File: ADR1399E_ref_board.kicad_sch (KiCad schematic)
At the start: 89 parts, among them J1 Conn_01x02_Pin, J2 USB_C_Receptacle_PowerOnly_6P, J3 Conn_Coaxial, J4 S4B-XH-A, P1 JST_B2P_VH, Q1 MMBT3906, U1 LT3042xMSE, U2 TPS61085DGK, U3 TL331, U4 ADR1399KEZ, U5 LMT01LPG, U6 OPA182IDR, U7 OPA994IDR

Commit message: Final BOM (?)
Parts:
- added C1, C22: 1uF 25V, Capacitor_SMD:C_0603_1608Metric_Pad1.08x0.95mm_HandSolder, symbol Device:C
- added D3, D4: LED, LED_SMD:LED_1206_3216Metric_Pad1.42x1.75mm_HandSolder, symbol Device:LED
- added R10: 0R, Resistor_SMD:R_0805_2012Metric_Pad1.20x1.40mm_HandSolder, symbol Device:R
- added R24: 180k 0.1%, Resistor_SMD:R_0603_1608Metric_Pad0.98x0.95mm_HandSolder, symbol Device:R
- added R28, R29: 1.5k 1/4W, Resistor_SMD:R_1206_3216Metric_Pad1.30x1.75mm_HandSolder, symbol Device:R
- C10: renamed from C9; Manufacturer_Name (none) -> Samsung Electro-Mechanics; Manufacturer_Part_Number (none) -> CL32A106KBJNNNE
- C11: renamed from C10; Manufacturer_Name (none) -> Samsung Electro-Mechanics; Manufacturer_Part_Number (none) -> CL32A106KBJNNNE
- C12: renamed from C11; value 100n 50V -> 100nF 50V; Manufacturer_Name (none) -> Samsung Electro-Mechanics; Manufacturer_Part_Number (none) -> CL10B104KB8NNWC
- C13: renamed from C12; Manufacturer_Name (none) -> Samsung Electro-Mechanics; Manufacturer_Part_Number (none) -> CL32A106KBJNNNE
- C14: renamed from C13; Manufacturer_Name (none) -> YAGEO; Manufacturer_Part_Number (none) -> CC0603JRNPO9BN821
- C15: renamed from C23; Manufacturer_Name (none) -> TAIYO YUDEN; Manufacturer_Part_Number (none) -> TMK107ABJ225KA-T
- C16: renamed from C24; value 100n 50V -> 100nF 50V; Manufacturer_Name (none) -> Samsung Electro-Mechanics; Manufacturer_Part_Number (none) -> CL10B104KB8NNWC
- C17: renamed from C14; value 100n 50V -> 100nF 50V; Manufacturer_Name (none) -> Samsung Electro-Mechanics; Manufacturer_Part_Number (none) -> CL10B104KB8NNWC
- C18: renamed from C15; Manufacturer_Name (none) -> TAIYO YUDEN; Manufacturer_Part_Number (none) -> TMK107ABJ225KA-T
- C19: Manufacturer_Name (none) -> TAIYO YUDEN; Manufacturer_Part_Number (none) -> TMK107ABJ225KA-T
- C2: renamed from C1; Manufacturer_Name (none) -> Samsung Electro-Mechanics; Manufacturer_Part_Number (none) -> CL21A106KPFNNNG
- C20: renamed from C16; value 100n 50V -> 100nF 50V; Manufacturer_Name (none) -> Samsung Electro-Mechanics; Manufacturer_Part_Number (none) -> CL10B104KB8NNWC
- C21: renamed from C17; Manufacturer_Name (none) -> TAIYO YUDEN; Manufacturer_Part_Number (none) -> TMK107ABJ225KA-T
- C23: renamed from C21; Manufacturer_Name (none) -> Murata; Manufacturer_Part_Number (none) -> GCM1885C1H302JA16D
- C24: renamed from C20; Manufacturer_Name (none) -> KEMET; Manufacturer_Part_Number (none) -> C0603C102J5GAC7411
- C3: renamed from C2; Manufacturer_Name (none) -> Samsung Electro-Mechanics; Manufacturer_Part_Number (none) -> CL21A106KPFNNNG
- C4: renamed from C3; Manufacturer_Name (none) -> Samsung Electro-Mechanics; Manufacturer_Part_Number (none) -> CL21A106KPFNNNG
- C5: renamed from C4; value 330n 50V -> 100nF 50V; Manufacturer_Name (none) -> Samsung Electro-Mechanics; Manufacturer_Part_Number (none) -> CL10B104KB8NNWC
- C6: renamed from C5; Manufacturer_Name (none) -> Samsung Electro-Mechanics; Manufacturer_Part_Number (none) -> CL32A106KBJNNNE
- C7: renamed from C6; Manufacturer_Name (none) -> KEMET; Manufacturer_Part_Number (none) -> A768KE157M1ELAE029
- C8: renamed from C7; value 330n 50V -> 100nF 50V; Manufacturer_Name (none) -> Samsung Electro-Mechanics; Manufacturer_Part_Number (none) -> CL10B104KB8NNWC
- C9: renamed from C8; Manufacturer_Name (none) -> Samsung Electro-Mechanics; Manufacturer_Part_Number (none) -> CL32A106KBJNNNE
- CR1, CR2, CR3: Manufacturer_Name (none) -> Toshiba; Manufacturer_Part_Number (none) -> CMS06(TE12L,Q,M)
- D1: Manufacturer_Name (none) -> Inolux; Manufacturer_Part_Number (none) -> IN-S126ATA
- J2: Manufacturer_Name (none) -> GCT; Manufacturer_Part_Number (none) -> USB4125-GF-A-0190
- J3: Manufacturer_Name (none) -> Molex; Manufacturer_Part_Number (none) -> 73251-1150
- J4: Manufacturer_Name (none) -> JST; Manufacturer_Part_Number (none) -> S4B-XH-A-GU
- L1: Manufacturer_Name (none) -> ABRACON; Manufacturer_Part_Number (none) -> ASPI-6045S-120M-T
- L2: Manufacturer_Name (none) -> TAIYO YUDEN; Manufacturer_Part_Number (none) -> LBC3225T1R5MR
- P1: Manufacturer_Name (none) -> JST; Manufacturer_Part_Number (none) -> B2P-VH-GU
- Q1: Manufacturer_Name (none) -> OnSemi; Manufacturer_Part_Number (none) -> MMBT3906LT1G
- R1: value 10k -> 10k 0.5% 25ppm; footprint Resistor_SMD:R_0805_2012Metric_Pad1.20x1.40mm_HandSolder -> Resistor_SMD:R_0603_1608Metric_Pad0.98x0.95mm_HandSolder; Manufacturer_Name (none) -> Vishay; Manufacturer_Part_Number (none) -> MCT06030D1002DP500
- R11: renamed from R19; Manufacturer_Name (none) -> Vishay; Manufacturer_Part_Number (none) -> MCU0805MZ0000ZP500
- R12: renamed from R20; Manufacturer_Name (none) -> Susumu; Manufacturer_Part_Number (none) -> RR1220Q-100-D
- R13: renamed from R12; value 200k -> 180k 0.1%; footprint Resistor_SMD:R_0805_2012Metric_Pad1.20x1.40mm_HandSolder -> Resistor_SMD:R_0603_1608Metric_Pad0.98x0.95mm_HandSolder; Manufacturer_Name (none) -> Panasonic; Manufacturer_Part_Number (none) -> ERA-3AEB184V
- R14: renamed from R10; footprint Resistor_SMD:R_0805_2012Metric_Pad1.20x1.40mm_HandSolder -> Resistor_SMD:R_0603_1608Metric_Pad0.98x0.95mm_HandSolder; Manufacturer_Name (none) -> KOA Speer; Manufacturer_Part_Number (none) -> RN73R1JTTD1004B25
- R15: renamed from R11; value 1.5k -> 1.5k 1/4W; footprint Resistor_SMD:R_0805_2012Metric_Pad1.20x1.40mm_HandSolder -> Resistor_SMD:R_1206_3216Metric_Pad1.30x1.75mm_HandSolder; Manufacturer_Name (none) -> SEI Stackpole; Manufacturer_Part_Number (none) -> RNCP1206FTD1K50
- R16: renamed from R13; footprint Resistor_SMD:R_0805_2012Metric_Pad1.20x1.40mm_HandSolder -> Resistor_SMD:R_0603_1608Metric_Pad0.98x0.95mm_HandSolder; Manufacturer_Name (none) -> KOA Speer; Manufacturer_Part_Number (none) -> RN73R1JTTD1004B25
- R17: renamed from R14; footprint Resistor_SMD:R_0805_2012Metric_Pad1.20x1.40mm_HandSolder -> Resistor_SMD:R_0603_1608Metric_Pad0.98x0.95mm_HandSolder; Manufacturer_Name (none) -> KOA Speer; Manufacturer_Part_Number (none) -> RN73R1JTTD1004B25
- R18: renamed from R22; Manufacturer_Name (none) -> YAGEO; Manufacturer_Part_Number (none) -> RT0805BRD071RL
- R19: renamed from R16; value 366k -> 180k 0.1%; footprint Resistor_SMD:R_0805_2012Metric_Pad1.20x1.40mm_HandSolder -> Resistor_SMD:R_0603_1608Metric_Pad0.98x0.95mm_HandSolder; Manufacturer_Name (none) -> Panasonic; Manufacturer_Part_Number (none) -> ERA-3AEB184V
- R2, R3: value 366k -> 180k 0.1%; footprint Resistor_SMD:R_0805_2012Metric_Pad1.20x1.40mm_HandSolder -> Resistor_SMD:R_0603_1608Metric_Pad0.98x0.95mm_HandSolder; Manufacturer_Name (none) -> Panasonic; Manufacturer_Part_Number (none) -> ERA-3AEB184V
- R20: renamed from R17; footprint Resistor_SMD:R_0805_2012Metric_Pad1.20x1.40mm_HandSolder -> Resistor_SMD:R_0603_1608Metric_Pad0.98x0.95mm_HandSolder; Manufacturer_Name (none) -> KOA Speer; Manufacturer_Part_Number (none) -> RN73R1JTTD1004B25
- R21: renamed from R24; value 10k 0.1% 10ppm -> 10k 0.5% 25ppm; footprint Resistor_SMD:R_0805_2012Metric_Pad1.20x1.40mm_HandSolder -> Resistor_SMD:R_0603_1608Metric_Pad0.98x0.95mm_HandSolder; Manufacturer_Name (none) -> Vishay; Manufacturer_Part_Number (none) -> MCT06030D1002DP500
- R22: renamed from R18; value 5R -> 4.99R; footprint Resistor_SMD:R_0805_2012Metric_Pad1.20x1.40mm_HandSolder -> Resistor_SMD:R_0603_1608Metric_Pad0.98x0.95mm_HandSolder; Manufacturer_Name (none) -> YAGEO; Manufacturer_Part_Number (none) -> RT0603DRE074R99L
- R23: Manufacturer_Name (none) -> TT Electronics; Manufacturer_Part_Number (none) -> PCF0603-13-1K0BT1
- R25: renamed from R15; Manufacturer_Name (none) -> Vishay; Manufacturer_Part_Number (none) -> MCU0805MZ0000ZP500
- R26: renamed from R25; footprint Resistor_SMD:R_0805_2012Metric_Pad1.20x1.40mm_HandSolder -> Resistor_SMD:R_0603_1608Metric_Pad0.98x0.95mm_HandSolder; Manufacturer_Name (none) -> YAGEO; Manufacturer_Part_Number (none) -> RT0603FRE077K5L
- R27: renamed from R26; value 100k -> 105k; footprint Resistor_SMD:R_0805_2012Metric_Pad1.20x1.40mm_HandSolder -> Resistor_SMD:R_0603_1608Metric_Pad0.98x0.95mm_HandSolder; Manufacturer_Name (none) -> YAGEO; Manufacturer_Part_Number (none) -> RT0603DRD07105KL
- R4, R5: footprint Resistor_SMD:R_0805_2012Metric_Pad1.20x1.40mm_HandSolder -> Resistor_SMD:R_0603_1608Metric_Pad0.98x0.95mm_HandSolder; Manufacturer_Name (none) -> Susumu; Manufacturer_Part_Number (none) -> RG1608P-512-D-T5
- R6: value 36k -> 17.8k 0.1%; footprint Resistor_SMD:R_0805_2012Metric_Pad1.20x1.40mm_HandSolder -> Resistor_SMD:R_0603_1608Metric_Pad0.98x0.95mm_HandSolder; Manufacturer_Name (none) -> Panasonic; Manufacturer_Part_Number (none) -> ERA-3AEB1782V
- R7: footprint Resistor_SMD:R_0805_2012Metric_Pad1.20x1.40mm_HandSolder -> Resistor_SMD:R_0603_1608Metric_Pad0.98x0.95mm_HandSolder; Manufacturer_Name (none) -> YAGEO; Manufacturer_Part_Number (none) -> RT0603DRD07105KL
- R8: value 10k -> 5.1k; footprint Resistor_SMD:R_0805_2012Metric_Pad1.20x1.40mm_HandSolder -> Resistor_SMD:R_0603_1608Metric_Pad0.98x0.95mm_HandSolder; Manufacturer_Name (none) -> Susumu; Manufacturer_Part_Number (none) -> RG1608P-512-D-T5
- R9: value 120k -> 120k 0.1%; footprint Resistor_SMD:R_0805_2012Metric_Pad1.20x1.40mm_HandSolder -> Resistor_SMD:R_0603_1608Metric_Pad0.98x0.95mm_HandSolder; Manufacturer_Name (none) -> Panasonic; Manufacturer_Part_Number (none) -> ERA-3AEB124V
- RN1: value 10k x8 -> 10k x8 5ppm reltol; Manufacturer_Name (none) -> Vishay; Manufacturer_Part_Number (none) -> NOMCT16031002AT1
- U1: Manufacturer_Name (none) -> Analog Devices Inc.; Manufacturer_Part_Number (none) -> LT3042EMSE#PBF
- U2: Manufacturer_Name (none) -> Texas Instruments; Manufacturer_Part_Number (none) -> TPS61085DGKR
- U3: renamed from U6; Manufacturer_Name (none) -> Texas Instruments; Manufacturer_Part_Number (none) -> OPA182IDR
- U4: renamed from U7; Manufacturer_Name (none) -> Texas Instruments; Manufacturer_Part_Number (none) -> OPA994IDR
- U5: renamed from U3; Manufacturer_Name (none) -> Texas Instruments; Manufacturer_Part_Number (none) -> TL331LVDBVR
- U6: renamed from U4; Manufacturer_Name (none) -> Analog Devices Inc.; Manufacturer_Part_Number (none) -> ADR1399KEZ
- U7: renamed from U5; Manufacturer_Name (none) -> Texas Instruments; Manufacturer_Part_Number (none) -> LMT01LPGM
- renumbered TP8 to TP7, TP9 to TP8, TP7 to TP9
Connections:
- net +5V: now also C1.1
- net +BATT: now also R28.1
- net Boost_En: now also R10.2; no longer R1.2, U2.3 (EN)
- net GND: now also C1.2, D3.1 (K), D4.1 (K), R24.2; no longer R19.2
- net Vref: now reaches C21.1, R13.2, R23.1, TP9.1, U3.3 (+IN), U6.6 (+REFF), U6.7 (+REFS)
- net Vref: now also C22.1
- net at C5.1, C6.1, C7.1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: now also R29.1
- net at C21.2, R22.1: now also C22.2
- new net: R19.2, R24.1
- new net: R1.2, R10.1, U2.3 (EN)
- new net: D4.2 (A), R29.2
- new net: D3.2 (A), R28.2
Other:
- moved on the sheet: CR2, CR3, R2, R6, TP9

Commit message: 3d model and footprint updates
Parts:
- CR1, CR2, CR3: footprint Snapeda:M-FLAT_TOS -> Samacsys:SODFL4724X108N
- L1: footprint Inductor_SMD:L_TDK_VLS6045EX_VLS6045AF -> Samacsys:ASPI-6045S
- U7: footprint Package_TO_SOT_THT:TO-92-2 -> Snapeda:LMT01LPG_LPG0002A
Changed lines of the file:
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@@
 			)
 		)
-		(property "Footprint" "Package_TO_SOT_THT:TO-92-2"
+		(property "Footprint" "Snapeda:LMT01LPG_LPG0002A"
 			(at 69.85 184.15 0)
 			(effects
@@
 			)
 		)
-		(property "Footprint" "Snapeda:M-FLAT_TOS"
+		(property "Footprint" "Samacsys:SODFL4724X108N"
 			(at 168.91 38.1 0)
 			(effects
@@
 			)
 		)
-		(property "Footprint" "Inductor_SMD:L_TDK_VLS6045EX_VLS6045AF"
+		(property "Footprint" "Samacsys:ASPI-6045S"
 			(at 96.52 41.91 0)
 			(effects
@@
 			)
 		)
-		(property "Footprint" "Snapeda:M-FLAT_TOS"
+		(property "Footprint" "Samacsys:SODFL4724X108N"
 			(at 121.92 52.07 0)
 			(effects
@@
 			)
 		)
-		(property "Footprint" "Snapeda:M-FLAT_TOS"
+		(property "Footprint" "Samacsys:SODFL4724X108N"
 			(at 171.45 52.07 0)
 			(effects

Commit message: more layout
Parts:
- removed CR1, CR2, CR3: CMS06TE12L_Q_M, Samacsys:SODFL4724X108N, symbol Snapeda:CMS06TE12L_Q_M
- added D5, D6, D7: CMS06_TE12L,Q,M_, Samacsys:SODFL4724X108N, symbol Samacsys:CMS06_TE12L,Q,M_
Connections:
- net +BATT: now also D5.2 (A)
- net Inductance: now also D5.1 (K)
- net at L1.2, U2.5 (SW): now also D7.2 (A)
- net at C5.1, C6.1, C7.1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: now also D6.2 (A), D7.1 (K)
- net at L2.1: now also D6.1 (K)

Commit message: Reference Island formed!
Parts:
- removed C22: 1uF 25V, Capacitor_SMD:C_0603_1608Metric_Pad1.08x0.95mm_HandSolder, symbol Device:C
- added H1, H2, H3, H4: MountingHole, MountingHole:MountingHole_3.2mm_M3_ISO7380, symbol Mechanical:MountingHole
- added H5, H6, H7, H8: MountingHole, MountingHole:MountingHole_2.2mm_M2, symbol Mechanical:MountingHole

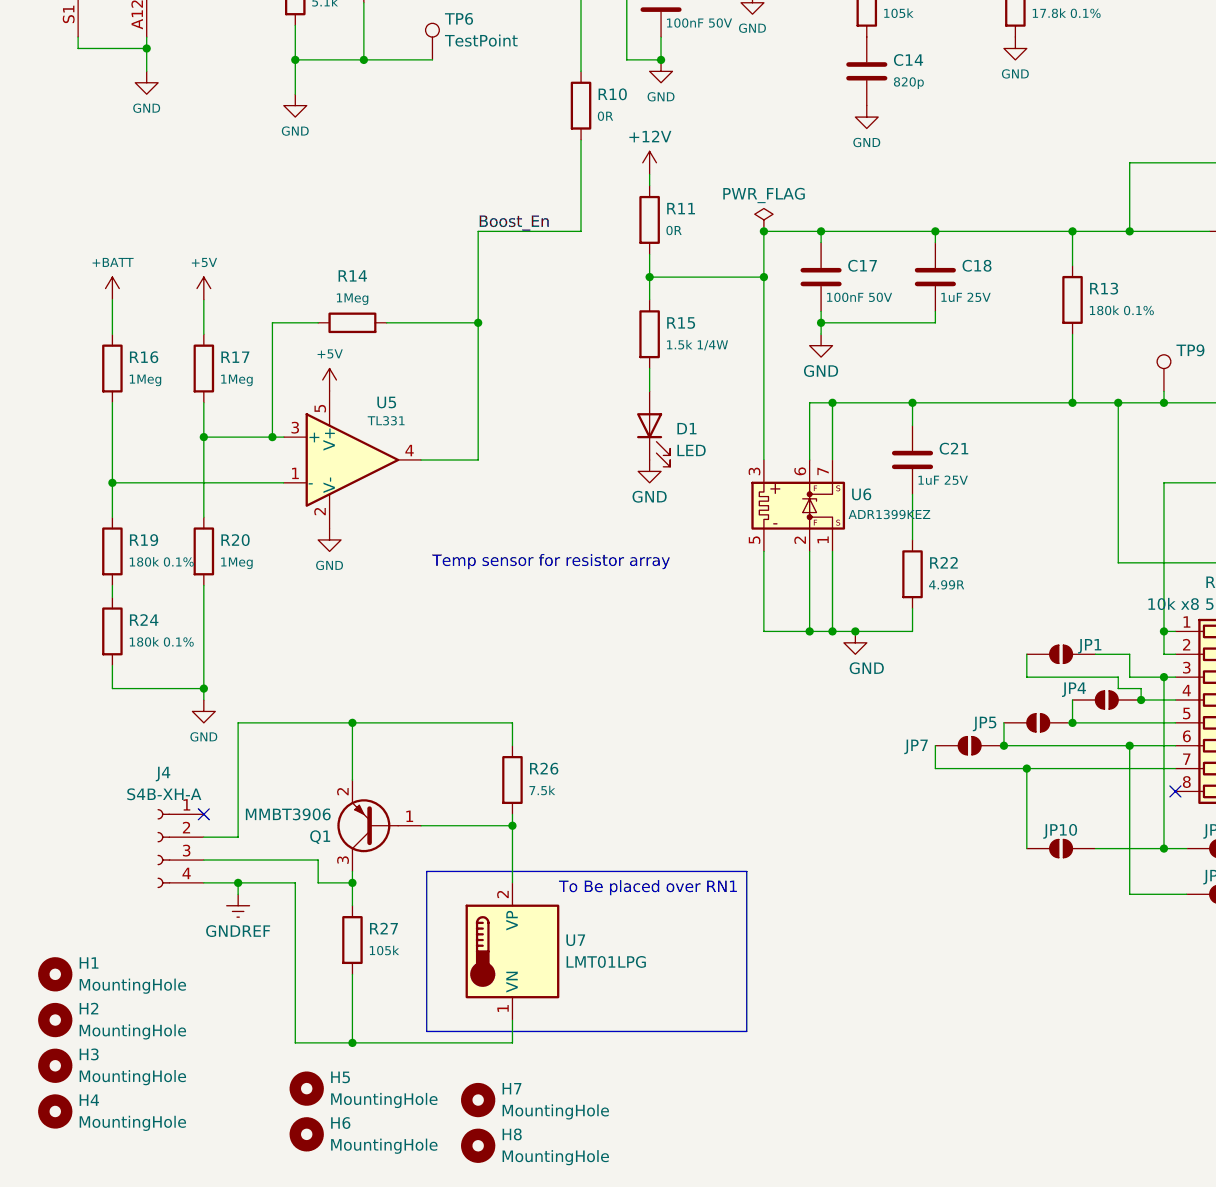
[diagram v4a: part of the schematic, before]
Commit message: initial amp placement
initial amp placement
Added Vbatt divider
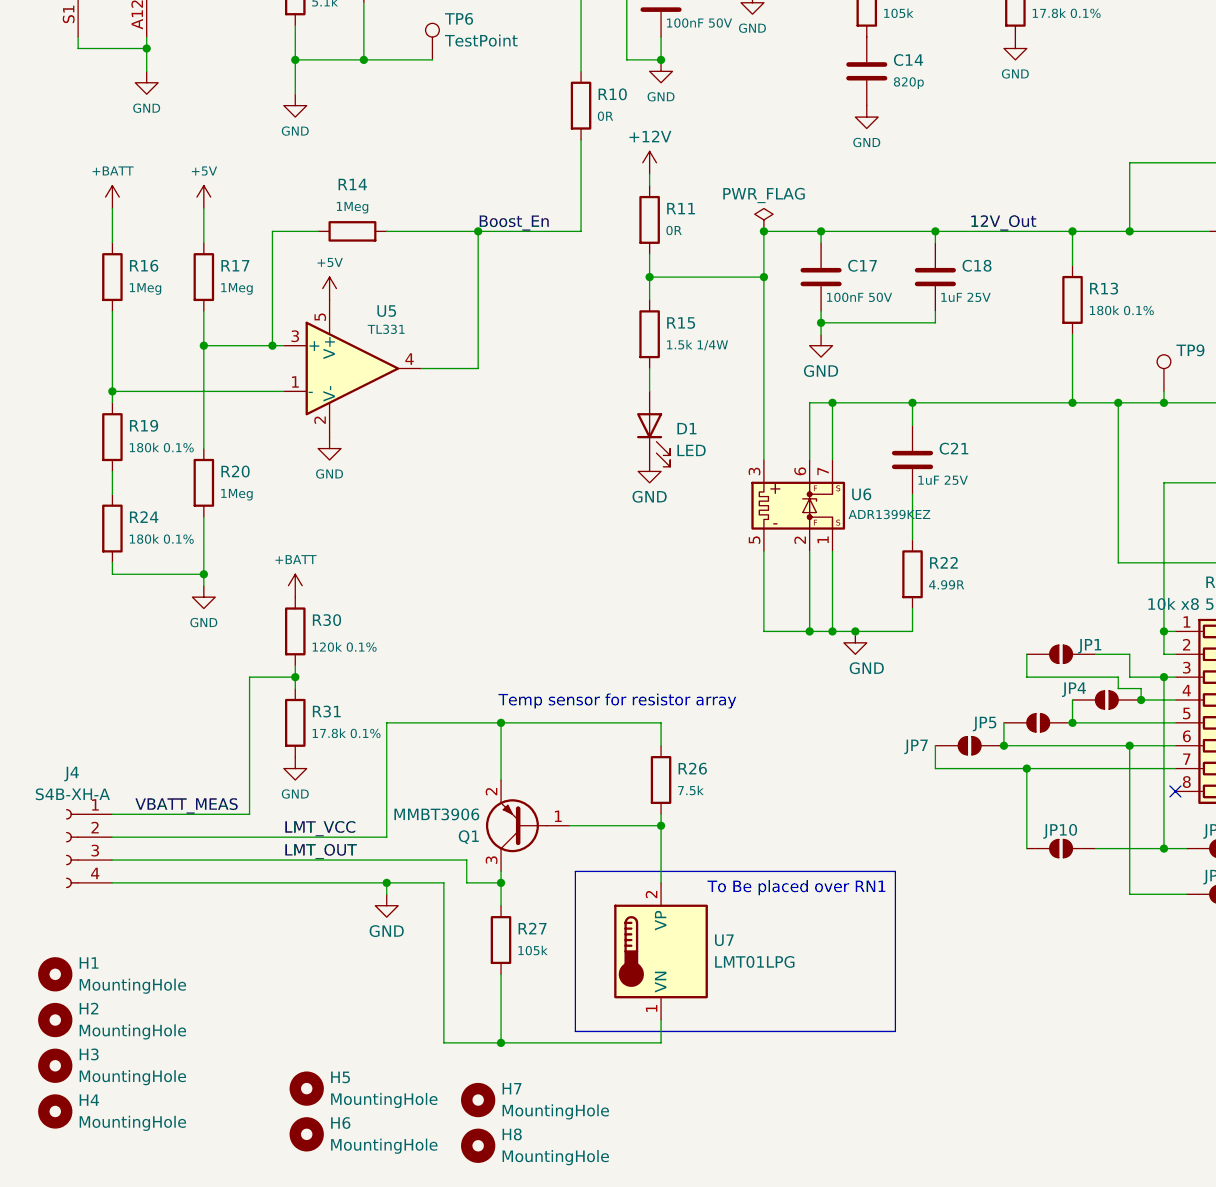
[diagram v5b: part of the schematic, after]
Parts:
- added R30: 120k 0.1%, Resistor_SMD:R_0603_1608Metric_Pad0.98x0.95mm_HandSolder, symbol Device:R
- added R31: 17.8k 0.1%, Resistor_SMD:R_0603_1608Metric_Pad0.98x0.95mm_HandSolder, symbol Device:R
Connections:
- net GNDREF is gone; now on net GND: J4.4 (Pin_4), R27.2, U7.1 (VN)
- net +BATT: now also R30.1
- net GND: now also R31.2
- net 12V_Out: now reaches C15.1, C16.1, C17.1, C18.1, R11.2, R12.1, R13.1, R15.1, U4.7 (V+), U6.3 (HEATER+)
- net LMT_VCC: now reaches J4.2 (Pin_2), Q1.2 (E), R26.1
- net VBATT_MEAS: now reaches J4.1 (Pin_1)
- net VBATT_MEAS: now also R30.2, R31.1
- net LMT_OUT: now reaches J4.3 (Pin_3), Q1.3 (C), R27.1
- no-connect marks 3 -> 2
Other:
- moved on the sheet: J4, Q1, R14, R16, R17, R19, R20, R24, R26, R27, U5, U7

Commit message: getting closer
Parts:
- J4: footprint Connector_JST:JST_XH_S4B-XH-A_1x04_P2.50mm_Horizontal -> Connector_JST:JST_XH_S4B-XH-A-1_1x04_P2.50mm_Horizontal
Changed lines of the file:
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@@
 			)
 		)
-		(property "Footprint" "Connector_JST:JST_XH_S4B-XH-A_1x04_P2.50mm_Horizontal"
+		(property "Footprint" "Connector_JST:JST_XH_S4B-XH-A-1_1x04_P2.50mm_Horizontal"
 			(at 20.32 161.29 0)
 			(effects

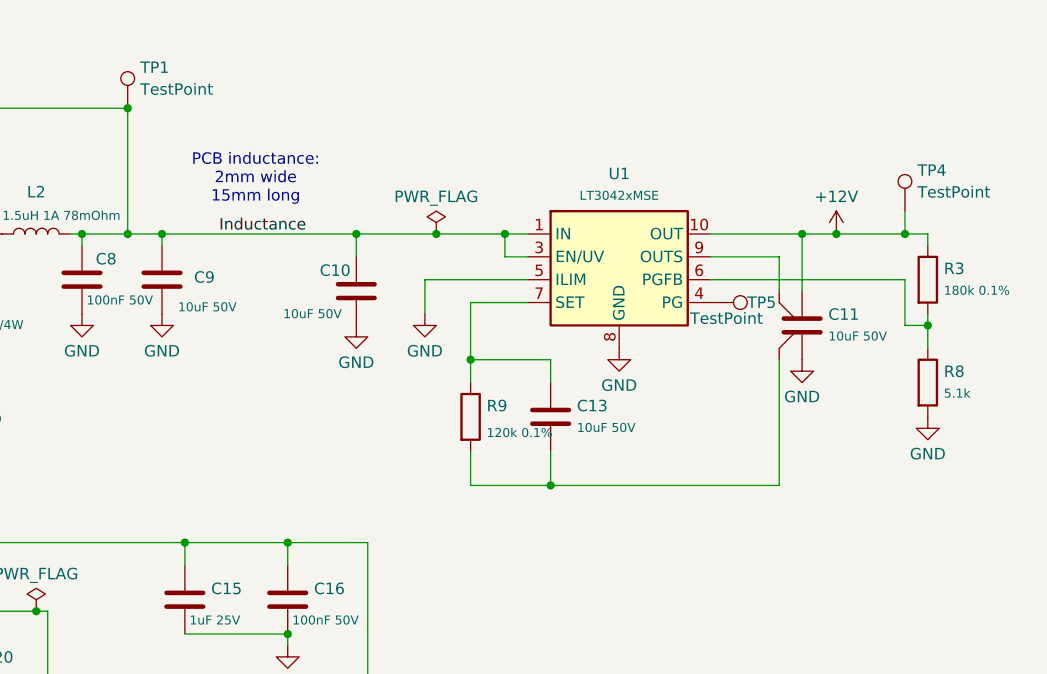
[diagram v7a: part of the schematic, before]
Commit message: moved from lt3042 to adp7118
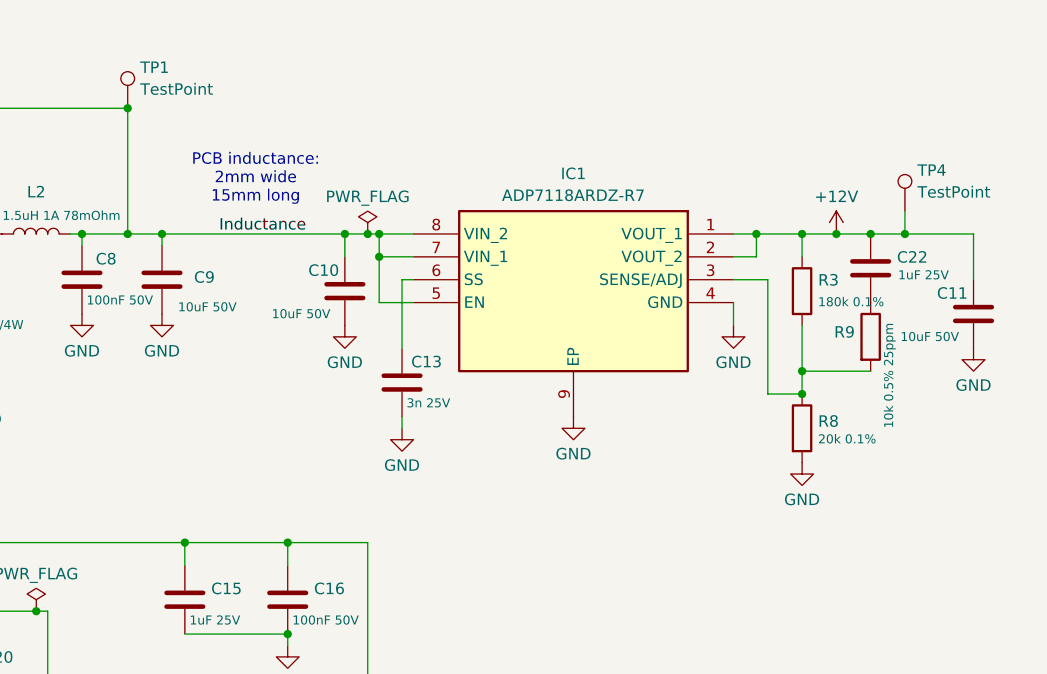
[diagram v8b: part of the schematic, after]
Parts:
- removed C11: 10uF 50V, nightmechanic_pcb:3225_Kelvin_4port, symbol nightmechanic_lib:Kelvin_Cap
- removed TP5: TestPoint, TestPoint:TestPoint_Pad_D1.5mm, symbol Connector:TestPoint
- removed U1: LT3042xMSE, Package_SO:MSOP-10-1EP_3x3mm_P0.5mm_EP1.68x1.88mm_ThermalVias, symbol Regulator_Linear:LT3042xMSE
- added C11: 10uF 50V, Capacitor_SMD:C_1210_3225Metric_Pad1.33x2.70mm_HandSolder, symbol Device:C
- added C22: 1uF 25V, Capacitor_SMD:C_0603_1608Metric_Pad1.08x0.95mm_HandSolder, symbol Device:C
- added IC1: ADP7118ARDZ-R7, Package_SO:SOIC-8-1EP_3.9x4.9mm_P1.27mm_EP2.29x3mm_ThermalVias, symbol Samacsys:ADP7118ARDZ-R7
- C13: value 10uF 50V -> 3n 25V; footprint Capacitor_SMD:C_1210_3225Metric_Pad1.33x2.70mm_HandSolder -> Capacitor_SMD:C_0603_1608Metric_Pad1.08x0.95mm_HandSolder; Manufacturer_Name Samsung Electro-Mechanics -> Murata; Manufacturer_Part_Number CL32A106KBJNNNE -> GCM1885C1H302JA16D
- R8: value 5.1k -> 20k 0.1%
- R9: value 120k 0.1% -> 10k 0.5% 25ppm; Manufacturer_Name Panasonic -> Vishay; Manufacturer_Part_Number ERA-3AEB124V -> MCT06030D1002DP500
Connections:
- net +12V: now also C11.1, C22.1, IC1.1 (VOUT_1), IC1.2 (VOUT_2)
- net GND: now also C13.2, C11.2, IC1.4 (GND), IC1.9 (EP)
- net Inductance: now also IC1.5 (EN), IC1.7 (VIN_1), IC1.8 (VIN_2)
- net at R3.2, R8.1: now also R9.2, IC1.3 (SENSE/ADJ)
- net at C13.1: now also IC1.6 (SS); no longer R9.1
- new net: C22.2, R9.1
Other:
- moved on the sheet: C10, R3, R8
